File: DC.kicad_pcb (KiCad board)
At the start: 4 copper layers, 196.5 x 181.5 mm, 87 parts, among them J1 348302001, J2 348302001, J3 757570141, J4 PPTC021LFBN-RC, U6 MCP2551-I-P, U7 NUCLEO-F302R8

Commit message: Updated pcb with new routing and gear select. Still errors to correct
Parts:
- removed the REF** at (285.0, 92.0)
- added R12: RC1206FR-0710KL, MiscellaneousLibrary:RESC3116X65N, F.Cu at (255.5, 62.4)
- added R14: RC1206FR-0710KL, MiscellaneousLibrary:RESC3116X65N, F.Cu at (250.5, 82.9)
- added R30: RC1206FR-0710KL, MiscellaneousLibrary:RESC3116X65N, F.Cu at (250.5, 62.4)
- added U8: 100DP6T1B1M1QEH, MiscellaneousLibrary:TO_1M1QEH_EWI, F.Cu at (250.7, 68.0)
- moved R11 18.9 mm to (121.5, 163.0), turned to 180 degrees
- moved J3 14.8 mm to (118.0, 187.0)
- moved F18 11.9 mm to (257.5, 116.0)
- moved F8 11.7 mm to (257.5, 99.0)
- moved F17 11.7 mm to (257.5, 111.5)
- moved F15 11.5 mm to (257.5, 103.0)
- moved F16 11.4 mm to (257.4, 107.0)
- moved U6 10.8 mm to (116.3, 155.2), turned to -90 degrees
- moved LED5 10.4 mm to (245.9, 116.0)
- moved R29 10.4 mm to (251.4, 116.0)
- moved LED1 10.2 mm to (245.9, 99.0)
- moved R19 10.2 mm to (251.3, 99.0)
- moved LED4 10.1 mm to (245.9, 111.5)
- moved R28 10.1 mm to (251.4, 111.5)
- moved R26 10.0 mm to (251.4, 103.0)
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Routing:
- net /HVILActive: track 1.52 -> 176.0 mm, vias 1 -> 2
- net /Neutral: track 0.00 -> 131.6 mm, vias 0 -> 1
- net /Drive: track 0.00 -> 128.7 mm, vias 0 -> 1
- net /Reverse: track 0.00 -> 123.3 mm, vias 0 -> 3
- net /RSignalLightIn: track 245.8 -> 177.2 mm, vias 4 -> 0
- net /From_PreChargeBtn: track 0.00 -> 43.3 mm, vias 0 -> 3
- net /To_ModeSelect: track 129.5 -> 151.9 mm
- net /CAN_RX: track 129.8 -> 108.2 mm
- net GND: track 35.3 -> 49.8 mm, vias 7 -> 22
- net /GreenLED1: track 46.6 -> 60.1 mm
- net /GreenLED2: track 43.4 -> 56.3 mm
- net +3.3V: track 9.92 -> 22.4 mm, vias 4 -> 10
- net /BlueLED5: track 72.9 -> 61.8 mm
- net /CAN_H: track 16.4 -> 27.1 mm
- net /BlueLED4: track 76.5 -> 66.1 mm, vias 1 -> 0
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- added copper zone on In1.Cu, net +3.3V
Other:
- board text added: "+12V"
- board text added: "BlueLEDS"
- board text added: "CAN-H"
- board text added: "CAN-L"
- board text added: "DashFault"
- board text added: "GND"
- board text added: "Gear Select"
- board text added: "GreenLEDS"
- board text added: "HV"
- board text added: "HVIL"
- board text added: "HVSwitch"
- board text added: "Hazard"
- board text added: "LCD"
- board text added: "LSignal"
- board text added: "LV"
- board text added: "LVSwitch"
- board text added: "ModeSelect"
- board text added: "PreCharge"
- board text added: "RSignal"

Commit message: VCU revisions, last review still to be done
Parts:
- removed C11: CL31B105KAHNNNE, Capacitor_SMD:CAPC3216X180N
- removed C12: C3216X7R2A474K160AA, Capacitor_SMD:CAPC3216X180N
- removed the F1 at (90.0, 140.5)
- removed the F2 at (90.0, 150.5)
- removed the F3 at (90.0, 161.0)
- removed the F4 at (90.5, 171.0)
- removed the F5 at (90.5, 181.0)
- removed the R18 at (228.0, 40.5)
- removed the R4 at (84.0, 171.0)
- removed the R5 at (84.0, 181.0)
- removed the R6 at (228.0, 29.5)
- removed the R7 at (228.0, 35.0)
- removed the REF** at (170.5, 107.0)
- removed the REF** at (190.5, 106.8)
- removed the U1 at (84.6, 146.8)
- removed the U5 at (84.5, 187.5)
- removed U8: 100DP6T1B1M1QEH, MiscellaneousLibrary:TO_1M1QEH_EWI
- added C1: C1206C104K5RACTU, DriverControlsLib:CAPC340180_88N_KEM, F.Cu at (246.0, 164.5)
- added C5: CL31B105KAHNNNE, DriverControlsLib:CAP_CL31_SAM, F.Cu at (114.4, 103.0)
- added C6: C1206C104K5RACTU, DriverControlsLib:CAPC340180_88N_KEM, F.Cu at (114.4, 99.0)
- added C8: CL31B225KBHNNNE, DriverControlsLib:CAP_CL31_SAM, F.Cu at (73.0, 79.5)
- added C8: CL31B225KBHNNNE, DriverControlsLib:CAP_CL31_SAM, B.Cu at (115.0, 92.5)
- added C9: C1206C104K5RACTU, DriverControlsLib:CAPC340180_88N_KEM, F.Cu at (190.0, 85.5)
- added F15: 0466.125NR, DriverControlsLib:0466Series_LTF, F.Cu at (176.7, 168.3)
- added F16: 0466.125NR, DriverControlsLib:0466Series_LTF, F.Cu at (189.7, 168.3)
- added F17: 0466.125NR, DriverControlsLib:0466Series_LTF, F.Cu at (203.2, 168.3)
- added F18: 0466.125NR, DriverControlsLib:0466Series_LTF, F.Cu at (216.7, 168.3)
- added F19: 0466.125NR, DriverControlsLib:0466Series_LTF, F.Cu at (230.2, 168.3)
- added Q1: BSS806NE, DriverControlsLib:SOT95P240X110-3N-1-V1, F.Cu at (181.2, 168.4)
- added Q2: BSS806NE, DriverControlsLib:SOT95P240X110-3N-1-V1, F.Cu at (194.2, 168.4)
- added Q3: BSS806NE, DriverControlsLib:SOT95P240X110-3N-1-V1, F.Cu at (207.6, 168.4)
- added Q4: BSS806NE, DriverControlsLib:SOT95P240X110-3N-1-V1, F.Cu at (221.1, 168.4)
- added Q5: BSS806NE, DriverControlsLib:SOT95P240X110-3N-1-V1, F.Cu at (234.7, 168.4)
- added R26: RC1206FR-0710KL, DriverControlsLib:RC1206N_YAG, F.Cu at (181.2, 177.8)
- added R27: RC1206FR-0710KL, DriverControlsLib:RC1206N_YAG, F.Cu at (194.5, 177.8)
- added R28: RC1206FR-0710KL, DriverControlsLib:RC1206N_YAG, F.Cu at (207.9, 177.8)
- added R29: RC1206FR-0710KL, DriverControlsLib:RC1206N_YAG, F.Cu at (221.3, 177.8)
- added R30: RC1206FR-0710KL, DriverControlsLib:RC1206N_YAG, F.Cu at (234.7, 177.8)
- added R31: RC1206JR-07120RL, DriverControlsLib:RC1206N_YAG, F.Cu at (181.2, 174.3)
- added R32: RC1206JR-07120RL, DriverControlsLib:RC1206N_YAG, F.Cu at (194.5, 174.3)
- added R33: RC1206JR-07120RL, DriverControlsLib:RC1206N_YAG, F.Cu at (207.9, 174.3)
- added R34: RC1206JR-07120RL, DriverControlsLib:RC1206N_YAG, F.Cu at (221.3, 174.3)
- added R35: RC1206JR-07120RL, DriverControlsLib:RC1206N_YAG, F.Cu at (234.7, 174.3)
- added REF**: MountingHole_4.5mm, MountingHole:MountingHole_4.5mm, F.Cu at (264.0, 64.0)
- added REF**: MountingHole_4.5mm, MountingHole:MountingHole_4.5mm, F.Cu at (75.5, 193.0)
- added REF**: MountingHole_4.5mm, MountingHole:MountingHole_4.5mm, F.Cu at (264.0, 193.0)
- added REF**: MountingHole_4.5mm, MountingHole:MountingHole_4.5mm, F.Cu at (75.5, 64.0)
- added U6: C1F 3, DriverControlsLib:C1_BEL, F.Cu at (258.0, 185.0)
- C2: renamed from C10; footprint Capacitor_SMD:CAPC3216X180N -> DriverControlsLib:CAP_CL31_SAM
- C3: renamed from C8; footprint Capacitor_SMD:CAPC3216X180N -> DriverControlsLib:CAP_CL31_SAM
- C4: renamed from C9; footprint Capacitor_SMD:CAPC3216X180N -> DriverControlsLib:CAP_CL31_SAM
- C7: value C -> CL31B105KAHNNNE; footprint DriverControlsLib:CAP-TH_L6.0-W3.5-P7.50-D1.0 -> DriverControlsLib:CAP_CL31_SAM
- D1: renamed from D2; footprint Fuse:Fuse_0603_1608Metric -> DriverControlsLib:LED_LTST-C_LTO
- D2: renamed from D4; footprint Fuse:Fuse_0603_1608Metric -> DriverControlsLib:LED_LTST-C_LTO
- D3: renamed from D5; footprint Fuse:Fuse_0603_1608Metric -> DriverControlsLib:LED_LTST-C_LTO
- D4: renamed from D6; footprint Fuse:Fuse_0603_1608Metric -> DriverControlsLib:LED_LTST-C_LTO
- D5: renamed from D7; footprint Fuse:Fuse_0603_1608Metric -> DriverControlsLib:LED_LTST-C_LTO
- D6: renamed from D9; footprint LED_SMD:LEDM1608X80 -> DriverControlsLib:LEDM1608X80
- D7: renamed from D8; footprint LED_SMD:LEDM1608X80 -> DriverControlsLib:LEDM1608X80
- D8: renamed from D1; footprint LED_SMD:LEDM1608X80 -> DriverControlsLib:LEDM1608X80
- D9: renamed from D3; footprint LED_SMD:LEDC1608X65N -> DriverControlsLib:LEDC1608X65N
- DS1: footprint Display:LCD_NHD-C0220BIZ-FSW-FBW-3V3M -> DriverControlsLib:NHD-C0220BIZ-FSW-FBW-3V3M_NDI
- F1: renamed from F8; footprint Fuse:FUSC3215X66N -> DriverControlsLib:0466Series_LTF
- F10: renamed from F9; footprint Fuse:FUSC3215X66N -> DriverControlsLib:0466Series_LTF
- F11, F12, F13, F14: footprint Fuse:FUSC3215X66N -> DriverControlsLib:0466Series_LTF
- F2: renamed from F15; footprint Fuse:FUSC3215X66N -> DriverControlsLib:0466Series_LTF
- F3: renamed from F16; footprint Fuse:FUSC3215X66N -> DriverControlsLib:0466Series_LTF
- F4: renamed from F17; footprint Fuse:FUSC3215X66N -> DriverControlsLib:0466Series_LTF
- F5: renamed from F18; footprint Fuse:FUSC3215X66N -> DriverControlsLib:0466Series_LTF
- F6: renamed from F20; footprint Fuse:FUSC3215X66N -> DriverControlsLib:0466Series_LTF
- F7: renamed from F19; footprint Fuse:FUSC3215X66N -> DriverControlsLib:0466Series_LTF
- F8: renamed from F7; footprint Fuse:FUSC3215X66N -> DriverControlsLib:0466Series_LTF
- F9: renamed from F10; footprint Fuse:FUSC3215X66N -> DriverControlsLib:0466Series_LTF
- J1, J2: footprint Connector_Molex:CONN_SD-34829-001_20_ST_MOL -> DriverControlsLib:CONN_SD-34829-001_20_ST_MOL; moved to B.Cu
- J3: footprint Connector_Molex:CONN_SD-75757-010_1X4_F11p20_MOL -> DriverControlsLib:CONN_SD-75757-010_1X4_F11p20_MOL; moved to B.Cu
- J4: footprint Connector:CONN2_LFBN-RC_SUL -> DriverControlsLib:CONN2_LFBN-RC_SUL
- LED1, LED2, LED3, LED4, LED5: footprint LED_SMD:LED_LTST-C170GKT_LTO -> DriverControlsLib:LED_LTST-C170GKT_LTO
- R1, R2, R3: value 220Ω -> RC1206FR-07665RL; footprint Resistor_SMD:RESC3216X70N -> DriverControlsLib:RC1206N_YAG
- R10: renamed from R19; footprint Resistor_SMD:RESC3116X65N -> DriverControlsLib:RESC3116X65N
- R11: renamed from R26; footprint Resistor_SMD:RESC3116X65N -> DriverControlsLib:RESC3116X65N
- R12: renamed from R27; footprint Resistor_SMD:RESC3116X65N -> DriverControlsLib:RESC3116X65N
- R13: renamed from R28; footprint Resistor_SMD:RESC3116X65N -> DriverControlsLib:RESC3116X65N
- R14: renamed from R29; footprint Resistor_SMD:RESC3116X65N -> DriverControlsLib:RESC3116X65N
- R15, R16, R17: footprint Resistor_SMD:RESC3116X65N -> DriverControlsLib:RC1206N_YAG
- R18: renamed from R10; footprint Resistor_SMD:RESC3116X65N -> DriverControlsLib:RC1206N_YAG
- R19: renamed from R8; footprint Resistor_SMD:RESC3116X65N -> DriverControlsLib:RC1206N_YAG
- R20: renamed from R9; footprint Resistor_SMD:RESC3116X65N -> DriverControlsLib:RC1206N_YAG
- R21: renamed from R12; footprint MiscellaneousLibrary:RESC3116X65N -> DriverControlsLib:RC1206N_YAG
- R22: renamed from R13; footprint Resistor_SMD:RESC3116X65N -> DriverControlsLib:RC1206N_YAG
- R23: renamed from R11; footprint Resistor_SMD:RESC3116X65N -> DriverControlsLib:RC1206N_YAG
- R24: renamed from R14; footprint MiscellaneousLibrary:RESC3116X65N -> DriverControlsLib:RC1206N_YAG
- R25: renamed from R30; footprint MiscellaneousLibrary:RESC3116X65N -> DriverControlsLib:RC1206N_YAG
- R4: renamed from R21; footprint Resistor_SMD:RESC3116X65N -> DriverControlsLib:RES_RC1206_YAG
- R5: renamed from R20; footprint Resistor_SMD:RESC3116X65N -> DriverControlsLib:RC1206N_YAG
- R6: renamed from R22; footprint Resistor_SMD:RESC3116X65N -> DriverControlsLib:RC1206N_YAG
- R7: renamed from R23; footprint Resistor_SMD:RESC3116X65N -> DriverControlsLib:RC1206N_YAG
- R8: renamed from R24; footprint Resistor_SMD:RESC3116X65N -> DriverControlsLib:RC1206N_YAG
- R9: renamed from R25; footprint Resistor_SMD:RESC3116X65N -> DriverControlsLib:RC1206N_YAG
- S1, S2, S3, S4: footprint Button_Switch_SMD:LP6OA2ASRG -> DriverControlsLib:LP6OA2ASRG
- S5: footprint Button_Switch_SMD:100SP1T8B13VS2REH -> DriverControlsLib:100SP1T8B13VS2REH
- U1: renamed from U6; footprint Package_DIP:DIP-8_W7.62mm -> DriverControlsLib:PDIP8_300MC_MCH
- U2: value ~ -> 100DP6T1B1M1QEH; footprint Battery:TO254P470X1016X2019-3P -> DriverControlsLib:TO_1M1QEH_EWI
- U3: footprint Battery:TO254P470X1016X2019-3P -> DriverControlsLib:LV_Switch
- U4: footprint Battery:TO254P470X1016X2019-3P -> DriverControlsLib:HV_Switch
- U5: renamed from U7; footprint Module:MODULE_NUCLEO-F302R8 -> DriverControlsLib:MODULE_NUCLEO-F302R8
- moved F7 172.4 mm to (80.6, 110.0), turned to 0 degrees
- moved F8 169.4 mm to (80.6, 114.5), turned to 0 degrees
- moved F9 168.9 mm to (80.6, 119.0), turned to 0 degrees
- moved F6 168.0 mm to (80.5, 105.5), turned to 0 degrees
- moved R4 157.8 mm to (88.1, 119.0), turned to 0 degrees
- moved R25 152.1 mm to (104.8, 106.2), turned to 90 degrees
- moved C3 152.0 mm to (153.4, 140.5), turned to -90 degrees
- moved D7 151.1 mm to (95.2, 110.0), turned to 180 degrees
- moved R24 150.0 mm to (104.8, 118.7), turned to 90 degrees
- moved D8 147.6 mm to (95.3, 114.5), turned to 180 degrees
- moved D9 147.1 mm to (95.3, 119.0), turned to 180 degrees
- moved S2 146.2 mm to (146.6, 137.5)
- moved D6 146.0 mm to (95.0, 105.2), turned to 180 degrees
- moved R16 144.5 mm to (153.4, 134.5), turned to 90 degrees
- moved R21 138.8 mm to (123.8, 106.2), turned to -90 degrees
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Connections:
- C7 pad 1: GND -> Net-(DS1-C1-)
- C7 pad 2: /CANTransceiver5V -> Net-(DS1-C1+)
- D1 pad 2: Net-(D2-Pad2) -> Net-(D1-Pad2)
- D2 pad 2: Net-(D4-Pad2) -> Net-(D2-Pad2)
- D3 pad 2: Net-(D5-Pad2) -> Net-(D3-Pad2)
- D4 pad 2: Net-(D6-Pad2) -> Net-(D4-Pad2)
- D5 pad 2: Net-(D7-Pad2) -> Net-(D5-Pad2)
- D6 pad A: Net-(D9-PadA) (its old number) -> Net-(D6-PadA)
- D7 pad A: Net-(D8-PadA) -> Net-(D7-PadA)
- D8 pad A: Net-(D1-PadA) -> Net-(D8-PadA)
- DS1 pad 1: Net-(DS1A-RST) -> Net-(DS1-ST)
- DS1 pad 7: Net-(DS1A-C1P) -> Net-(DS1-C1+)
- DS1 pad 8: Net-(DS1A-C1N) -> Net-(DS1-C1-)
- F10 pad 2: Net-(F9-Pad2) (its old number) -> Net-(F10-Pad2)
- F6 pad 2: Net-(F20-Pad2) -> Net-(F6-Pad2)
- F7 pad 2: Net-(F19-Pad2) -> Net-(F7-Pad2)
- F8 pad 2: Net-(F7-Pad2) -> Net-(F8-Pad2)
- J1 pad 1: /To_PreChargeBtn -> /HVSwitch+
- J1 pad 10: /GreenLED2 -> /BlueLED1
- J1 pad 11: /GreenLED3 -> /To_PreChargeBtn
- J1 pad 12: /GreenLED4 -> /Enable
- J1 pad 13: /GreenLED5 -> /Enable
- J1 pad 14: /LVSwitch+ -> /ChargeMode
- J1 pad 15: /LVSwitch- -> /To_ModeSelect
- J1 pad 16: /HVSwitch+ -> /ReadyMode
- J1 pad 17: /HVSwitch- -> /LVActive
- J1 pad 18: /To_ModeSelect -> /HVActive
- J1 pad 19: /ReadyMode -> /HVILActive
- J1 pad 2: /From_PreChargeBtn -> /HVSwitch-
- J1 pad 20: GND -> /DashFaultIndicator
- J1 pad 3: /Enable -> /LVSwitch+
- J1 pad 4: /BlueLED1 -> /LVSwitch-
- J1 pad 5: /BlueLED2 -> GND
- J1 pad 6: /BlueLED3 -> /BlueLED5
- J1 pad 8: /BlueLED5 -> /BlueLED3
- J1 pad 9: /GreenLED1 -> /BlueLED2
- J2 pad 1: /ChargeMode -> /LSignalLightNeg
- J2 pad 10: /BrakeLightNeg -> /GreenLED2
- J2 pad 13: /LSignalLightNeg -> /RSignalLightNeg
- J2 pad 14: /LSignalLightNeg -> /BrakeLightNeg
- J2 pad 15: /LSignalLightNeg -> /BrakeLightNeg
- J2 pad 16: /RSignalLightNeg -> /BrakeLightNeg
- J2 pad 17: /RSignalLightNeg -> GND
- J2 pad 18: /RSignalLightNeg -> /GreenLED5
- J2 pad 19: /ThermalShutoff -> /GreenLED4
- J2 pad 2: /LVActive -> /LSignalLightNeg
- J2 pad 20: GND -> /GreenLED3
- J2 pad 3: /HVActive -> /LSignalLightNeg
- J2 pad 4: /DashFaultIndicator -> /RSignalLightNeg
- J2 pad 5: /HVILActive -> /RSignalLightNeg
- J2 pad 6: /AccelIn -> /ThermalShutoff
- J2 pad 7: /BrakeLightIn -> /BrakePedalIn
- J2 pad 8: /BrakeLightNeg -> /AccelIn
- J2 pad 9: /BrakeLightNeg -> /GreenLED1
- R1 pad 1: Net-(U1-G) -> Net-(D6-PadA)
- R1 pad 2: /BrakeLightOut -> Net-(F6-Pad2)
- R15 pad 1: +3.3V -> /HazardIn
- R15 pad 2: /HazardIn -> +3.3V
- R16 pad 1: +3.3V -> /RSignalLightIn
- R16 pad 2: /RSignalLightIn -> +3.3V
- R17 pad 1: +3.3V -> /LSignalLightIn
- R17 pad 2: /LSignalLightIn -> +3.3V
- R18 pad 1: GND -> Net-(DS1-ST)
- R18 pad 2: Net-(DS1A-RST) -> GND
- R19 pad 1: +3.3V -> /I2C1_CLK
- R19 pad 2: /I2C1_CLK -> +3.3V
- R2 pad 1: Net-(U2-G) -> Net-(D7-PadA)
- R2 pad 2: /RSignalLightOut -> Net-(F7-Pad2)
- R20 pad 1: +3.3V -> /I2C1_SDA
- R20 pad 2: /I2C1_SDA -> +3.3V
- R21 pad 1: /Reverse -> +3.3V
- R21 pad 2: +3.3V -> /Reverse
- R22 pad 1: Net-(J4-Pad2) -> /CAN_L
- R22 pad 2: /CAN_L -> Net-(J4-Pad2)
- R23 pad 1: GND -> Net-(U1-RS)
- R23 pad 2: Net-(U6-Rs) -> GND
- R24 pad 1: /Drive -> +3.3V
- R24 pad 2: +3.3V -> /Drive
- R25 pad 1: +3.3V -> /Neutral
- R25 pad 2: /Neutral -> +3.3V
- R3 pad 1: Net-(U3-G) -> Net-(D8-PadA)
- R3 pad 2: /LSignalLightOut -> Net-(F8-Pad2)
- R5 pad 1: Net-(F9-Pad2) (its old number) -> Net-(D1-Pad2)
- R5 pad 2: Net-(D2-Pad2) -> Net-(F10-Pad2)
- R6 pad 1: Net-(F11-Pad2) -> Net-(D2-Pad2)
- R6 pad 2: Net-(D4-Pad2) -> Net-(F11-Pad2)
- R7 pad 1: Net-(F12-Pad2) -> Net-(D3-Pad2)
- R7 pad 2: Net-(D5-Pad2) -> Net-(F12-Pad2)
- R8 pad 1: Net-(F13-Pad2) -> Net-(D4-Pad2)
- R8 pad 2: Net-(D6-Pad2) -> Net-(F13-Pad2)
- R9 pad 1: Net-(F14-Pad2) -> Net-(D5-Pad2)
- R9 pad 2: Net-(D7-Pad2) -> Net-(F14-Pad2)
- S1 pad MH1: unconnected-(S1-PadMH1) -> GND
- S1 pad MH2: unconnected-(S1-PadMH2) -> GND
- S1 pad MH3: unconnected-(S1-PadMH3) -> GND
- S1 pad MH4: unconnected-(S1-PadMH4) -> GND
- S2 pad MH1: unconnected-(S2-PadMH1) -> GND
- S2 pad MH2: unconnected-(S2-PadMH2) -> GND
- S2 pad MH3: unconnected-(S2-PadMH3) -> GND
- S2 pad MH4: unconnected-(S2-PadMH4) -> GND
- S3 pad MH1: unconnected-(S3-PadMH1) -> GND
- S3 pad MH2: unconnected-(S3-PadMH2) -> GND
- S3 pad MH3: unconnected-(S3-PadMH3) -> GND
- S3 pad MH4: unconnected-(S3-PadMH4) -> GND
- S4 pad 2: /From_PreChargeBtn -> /Enable
- S4 pad MH1: unconnected-(S4-PadMH1) -> GND
- S4 pad MH2: unconnected-(S4-PadMH2) -> GND
- S4 pad MH3: unconnected-(S4-PadMH3) -> GND
- S4 pad MH4: unconnected-(S4-PadMH4) -> GND
- S5 pad 1: unconnected-(S5-NC-Pad1) -> /ChargeMode
- S5 pad 4: unconnected-(S5-MH1-Pad4) -> GND
- S5 pad 5: unconnected-(S5-MH2-Pad5) -> GND
- S5 pad 6: unconnected-(S5-MH3-Pad6) -> GND
- S5 pad 7: unconnected-(S5-MH4-Pad7) -> GND
- U1 pad 8: Net-(U6-Rs) -> Net-(U1-RS)
- U2 pad 1: Net-(U2-G) -> /Reverse
- U2 pad 2: Net-(U2-D) -> GND
- U2 pad 3: GND -> Net-(U2-Pad3)
- U3 pad 1: Net-(U3-G) -> /LVSwitch+
- U3 pad 2: Net-(U3-D) -> /LVSwitch-
- U4 pad 1: Net-(U4-G) -> /HVSwitch+
- U4 pad 2: Net-(U4-D) -> /HVSwitch-
- U5 pad CN10_16: /DRLRightOut -> /DRLLeftOut
- U5 pad CN10_18: /LSignalLightOut -> /DRLRightOut
- U5 pad CN10_2: /BrakeLightOut -> unconnected-(U5B-PC8-PadCN10_2)
- U5 pad CN10_20: unconnected-(U7B-GND_CN10_20-PadCN10_20) -> GND
- U5 pad CN10_21: /BrakePedalIn -> unconnected-(U5B-PA9-PadCN10_21)
- U5 pad CN10_22: unconnected-(U7B-PB2-PadCN10_22) -> /LSignalLightOut
- U5 pad CN10_24: /RSignalLightIn -> /RSignalLightOut
- U5 pad CN10_25: /LSignalLightIn -> unconnected-(U5B-PB10-PadCN10_25)
- U5 pad CN10_26: /Drive -> /BrakeLightOut
- U5 pad CN10_27: unconnected-(U7B-PB4-PadCN10_27) -> /Reverse
- U5 pad CN10_28: /Neutral -> /ThermalShutoff
- U5 pad CN10_29: unconnected-(U7B-PB5-PadCN10_29) -> /Neutral
- U5 pad CN10_30: /Reverse -> /BrakePedalIn
- U5 pad CN10_31: unconnected-(U7B-PB3-PadCN10_31) -> /Drive
- U5 pad CN10_33: /ThermalShutoff -> /LSignalLightIn
- U5 pad CN10_35: /UART_TX -> /HazardIn
- U5 pad CN10_37: /UART_RX -> /RSignalLightIn
- U5 pad CN10_4: /RSignalLightOut -> unconnected-(U5B-PC6-PadCN10_4)
- U5 pad CN10_6: /DRLLeftOut -> unconnected-(U5B-PC5-PadCN10_6)
- U5 pad CN7_32: /DIExtra1 -> unconnected-(U5A-PA4-PadCN7_32)
- U5 pad CN7_34: /DIExtra2 -> unconnected-(U5A-PB0-PadCN7_34)
- U5 pad CN7_36: /DOExtra1 -> unconnected-(U5A-PC1-PadCN7_36)
- U5 pad CN7_38: /HazardIn -> unconnected-(U5A-PC0-PadCN7_38)
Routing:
- net /RSignalLightIn: track 177.2 -> 38.3 mm
- net Net-(U5A-VIN): track 0.00 -> 129.0 mm
- net /DRLRightOut: track 154.5 -> 41.8 mm, vias 3 -> 0
- net /DRLLeftOut: track 153.6 -> 45.8 mm, vias 2 -> 0
- net /LSignalLightOut: track 143.6 -> 37.6 mm, vias 3 -> 0
- net /ChargeMode: track 0.00 -> 92.9 mm
- net /DashFaultIndicator: track 165.6 -> 82.7 mm, vias 2 -> 0
- net /HVILActive: track 176.0 -> 94.2 mm, vias 2 -> 0
- net /AccelIn: track 41.8 -> 121.6 mm, vias 2 -> 1
- net /HVActive: track 189.1 -> 110.3 mm
- net /LSignalLightNeg: track 104.3 -> 26.8 mm, vias 4 -> 0
- net /RSignalLightOut: track 112.6 -> 35.8 mm, vias 1 -> 0
- net /HVSwitch-: track 104.1 -> 27.7 mm, vias 1 -> 0
- net /RSignalLightNeg: track 106.6 -> 30.9 mm, vias 4 -> 0
- net /DRLRightNeg: track 97.4 -> 27.3 mm, vias 2 -> 0
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- removed copper zone on In1.Cu, net (none)
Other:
- board size 196.5 x 181.5 mm -> 199.5 x 140 mm
- board text added: "1"
- board text added: "10"
- board text added: "11"
- board text added: "20"
- board text added: "Blue LEDs"
- board text added: "CANH"
- board text added: "CANL"
- board text added: "Green LEDs"
- board text added: "HV Switch"
- board text added: "LV Switch"
- board text added: "Left Signal"
- board text added: "Mode Select"
- board text added: "Pre-charge"
- board text added: "Right Signal"
- board text added: "SUNSTANG"
- board text added: "Sunstang VCU 2026 Hanjing Lin Sahil Sharma Xiuting Shi"
- board text removed: "BlueLEDS"
- board text removed: "CAN-H"
- board text removed: "CAN-L"
- board text removed: "DashFault"
- board text removed: "GreenLEDS"
- board text removed: "HV"
- board text removed: "HVIL"
- board text removed: "HVSwitch"
- board text removed: "LCD"
- board text removed: "LSignal"
- board text removed: "LV"
- board text removed: "LVSwitch"
- board text removed: "ModeSelect"
- board text removed: "PreCharge"
- board text removed: "RSignal"

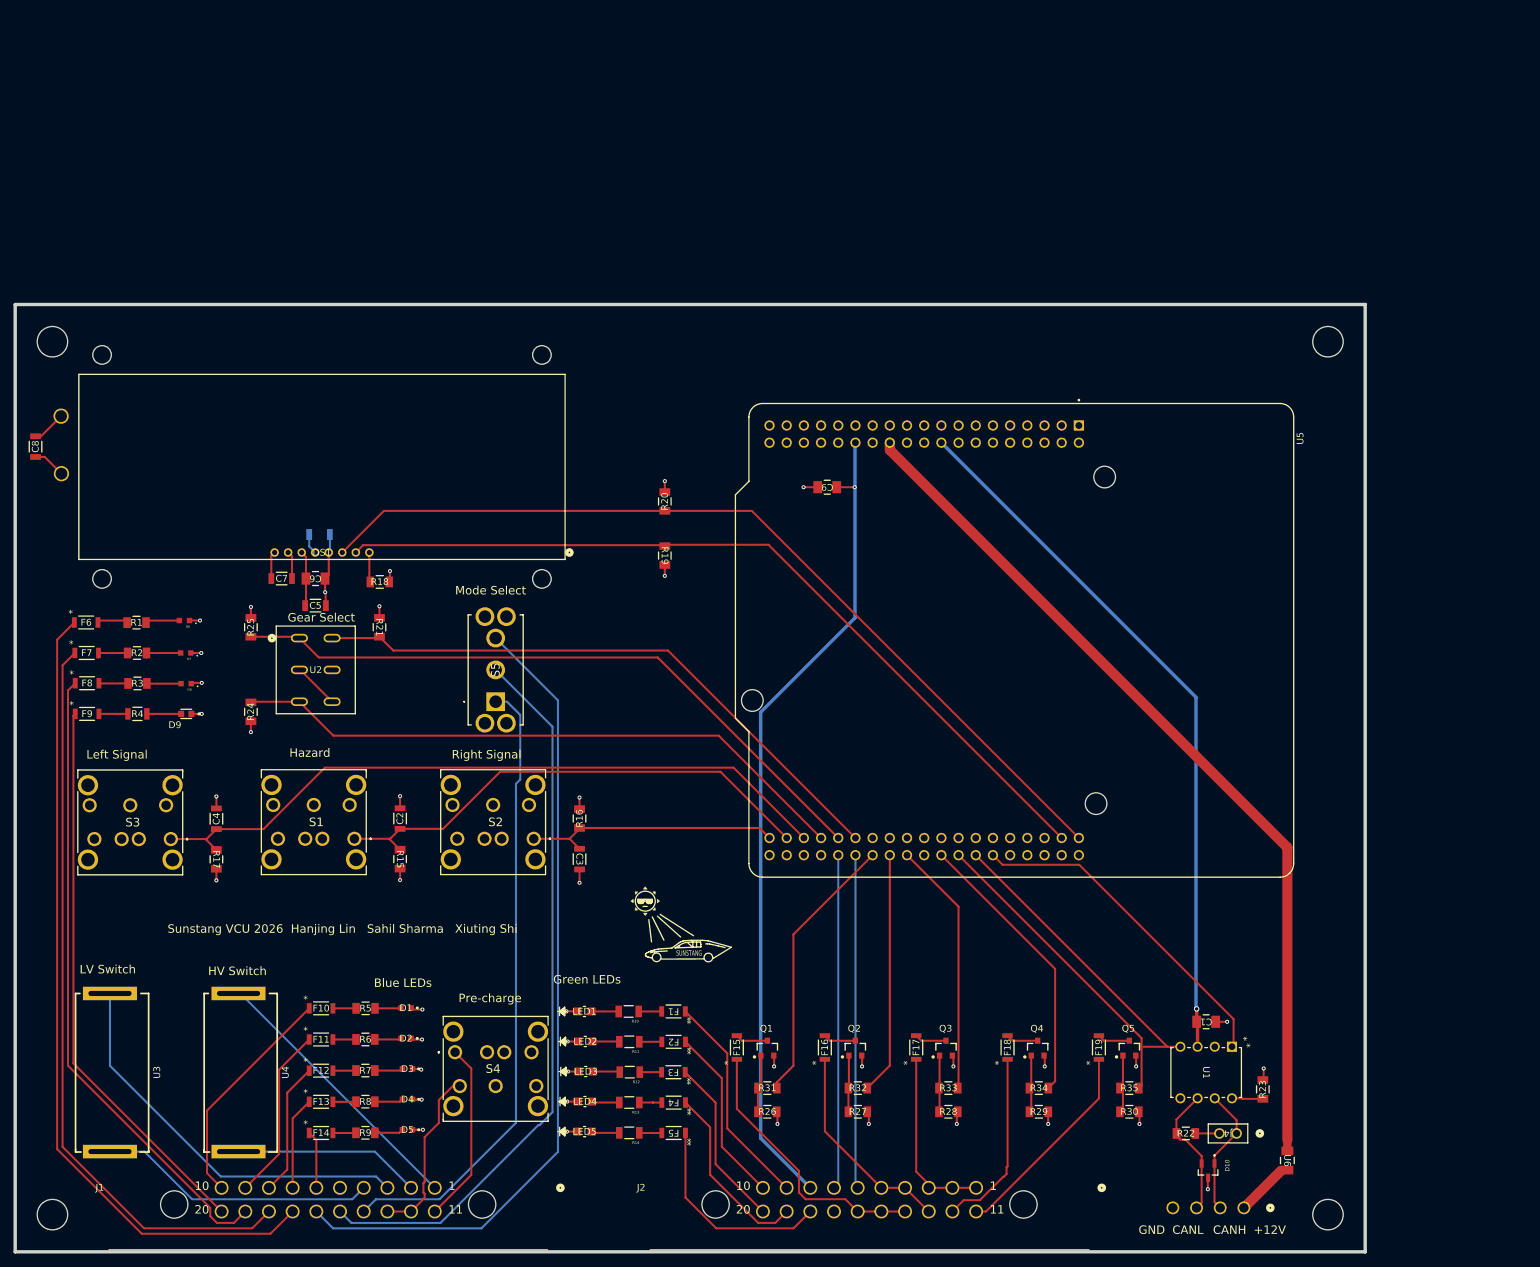
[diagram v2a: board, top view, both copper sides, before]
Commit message: small corrections, added voltage divider for BreakPedalIn
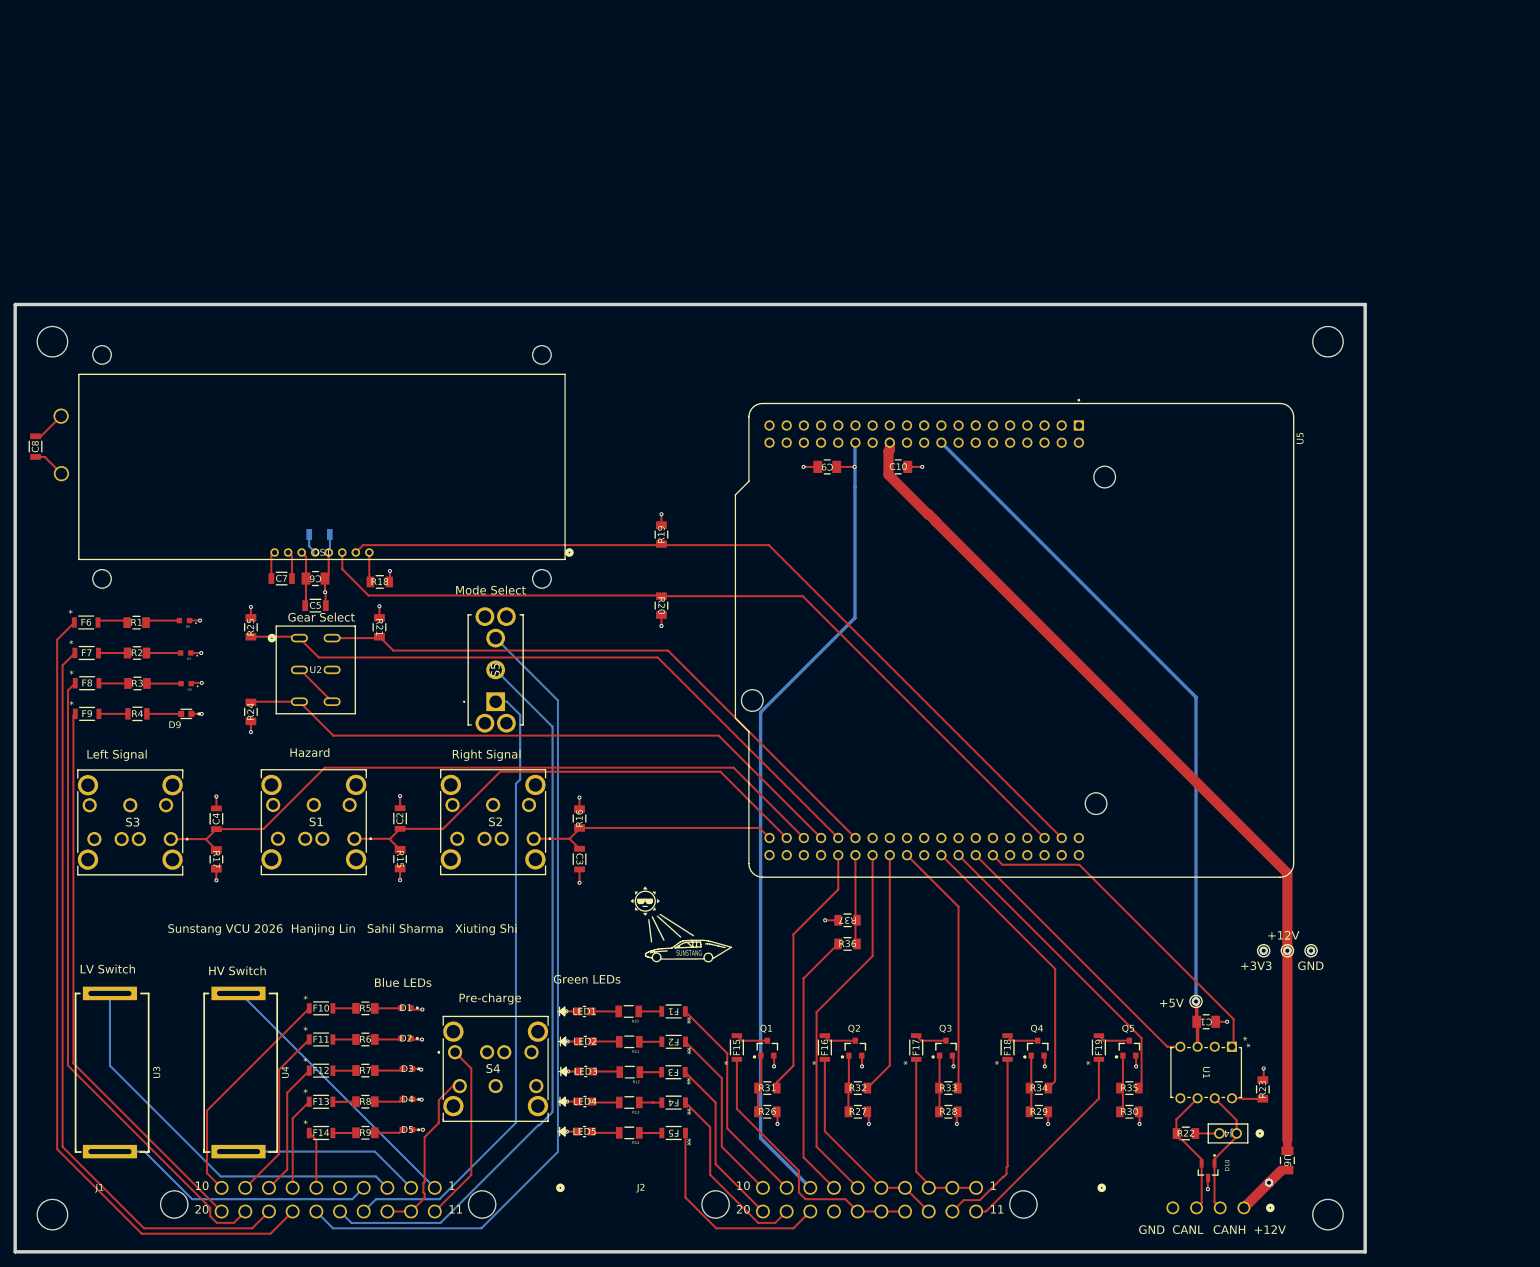
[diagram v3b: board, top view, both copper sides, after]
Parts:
- added C10: C1206C104K5RACTU, DriverControlsLib:CAPC340180_88N_KEM, F.Cu at (200.5, 82.5)
- added R36: RC1206FR-0710KL, DriverControlsLib:RC1206N_YAG, F.Cu at (193.0, 153.0)
- added R37: RC1206FR-073K3L, DriverControlsLib:RC1206N_YAG, F.Cu at (193.0, 149.5)
- moved R20 15.4 mm to (165.5, 103.0), turned to -90 degrees
- moved R19 3.14 mm to (165.5, 92.5), turned to 90 degrees
- moved C9 3.00 mm to (190.0, 82.5)
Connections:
- net /I2C1_CLK renamed /I2C1_SCL
- net /To_PreChargeBtn renamed /From_PreChargeBtn
- R21 pad 2: /Reverse -> /Drive
- R24 pad 2: /Drive -> /Reverse
- U2 pad 1: /Reverse -> /Drive
- U2 pad 6: /Drive -> /Reverse
- U5 pad CN10_1: /I2C1_SDA -> unconnected-(U5B-PC9-PadCN10_1)
- U5 pad CN10_26: /BrakeLightOut -> /ThermalShutoff
- U5 pad CN10_27: /Reverse -> /Drive
- U5 pad CN10_28: /ThermalShutoff -> Net-(U5B-PA6)
- U5 pad CN10_30: /BrakePedalIn -> /BrakeLightOut
- U5 pad CN10_31: /Drive -> /Reverse
- U5 pad CN10_5: unconnected-(U5B-PB9-PadCN10_5) -> /I2C1_SDA
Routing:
- net Net-(U5B-PA6): track 0.00 -> 13.2 mm
- net /I2C1_SDA: track 131.4 -> 122.7 mm
- net /BrakePedalIn: track 49.4 -> 40.9 mm
- net /ThermalShutoff: track 49.3 -> 55.6 mm
- net GND: track 67.1 -> 70.8 mm, vias 33 -> 36
- net /CAN_RX: track 45.5 -> 42.0 mm
- net /Reverse: track 89.7 -> 92.6 mm
- net /Drive: track 92.6 -> 89.7 mm
- net /BrakeLightOut: track 40.3 -> 38.2 mm
- net /CAN_L: track 20.0 -> 19.5 mm
- net Net-(U5A-VIN): track 129.0 -> 129.2 mm, vias 0 -> 1
- net +3.3V: vias 8 -> 9
- net +12V: vias 0 -> 1
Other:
- board text added: "+3V3"
- board text added: "+5V"
